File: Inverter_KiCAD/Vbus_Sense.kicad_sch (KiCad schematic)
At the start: 9 parts, among them U12 HCPL-7800A

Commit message: assigments footprints
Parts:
- removed U5: ~, symbol MPRB2415S-6W:MPRB2415S-6W
- C10: footprint (none) -> Capacitor_SMD:CP_Elec_6.3x7.7; MFR (none) -> 865060445005
- C19: footprint (none) -> Capacitor_SMD:CP_Elec_5x5.4; MFR (none) -> 865060442002
- C24, C27, C30: footprint (none) -> Capacitor_SMD:C_0603_1608Metric_Pad1.08x0.95mm_HandSolder
- R13, R16: footprint (none) -> Resistor_SMD:R_0603_1608Metric_Pad0.98x0.95mm_HandSolder
- U12: footprint 300mil_DIP-8_BRA -> HCPL-7800A:HCPL-7800A
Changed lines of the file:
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@@
       (effects (font (size 1.27 1.27)) (justify left))
     )
-    (property "Footprint" "" (at 118.11 73.66 0)
+    (property "Footprint" "Capacitor_SMD:C_0603_1608Metric_Pad1.08x0.95mm_HandSolder" (at 118.11 73.66 0)
       (effects (font (size 1.27 1.27)) hide)
     )
@@
         )
         (path "/5e6c1e3f-0815-454a-8acb-8e3e2d064875/68381f6c-5b48-4aca-8792-bde0d1e54d5e"
-          (reference "C33") (unit 1)
+          (reference "C35") (unit 1)
         )
       )
@@
         )
         (path "/5e6c1e3f-0815-454a-8acb-8e3e2d064875/68381f6c-5b48-4aca-8792-bde0d1e54d5e"
-          (reference "#PWR023") (unit 1)
+          (reference "#PWR036") (unit 1)
         )
       )
@@
       (effects (font (size 1.27 1.27)) (justify left))
     )
-    (property "Footprint" "" (at 47.9552 104.14 0)
+    (property "Footprint" "Capacitor_SMD:CP_Elec_6.3x7.7" (at 47.9552 104.14 0)
       (effects (font (size 1.27 1.27)) hide)
     )
@@
       (effects (font (size 1.27 1.27)) hide)
     )
+    (property "MFR" "865060445005" (at 46.99 100.33 0)
+      (effects (font (size 1.27 1.27)) hide)
+    )
     (pin "1")
     (pin "2")
@@
         )
         (path "/5e6c1e3f-0815-454a-8acb-8e3e2d064875/68381f6c-5b48-4aca-8792-bde0d1e54d5e"
-          (reference "C36") (unit 1)
+          (reference "C33") (unit 1)
         )
       )
@@
         )
         (path "/5e6c1e3f-0815-454a-8acb-8e3e2d064875/68381f6c-5b48-4aca-8792-bde0d1e54d5e"
-          (reference "#PWR045") (unit 1)
+          (reference "#PWR032") (unit 1)
         )
       )
@@
       (effects (font (size 1.524 1.524)))
     )
-    (property "Footprint" "300mil_DIP-8_BRA" (at 146.05 85.09 0)
+    (property "Footprint" "HCPL-7800A:HCPL-7800A" (at 146.05 85.09 0)
       (effects (font (size 1.27 1.27) italic) hide)
     )
@@
         )
         (path "/5e6c1e3f-0815-454a-8acb-8e3e2d064875/68381f6c-5b48-4aca-8792-bde0d1e54d5e"
-          (reference "U15") (unit 1)
+          (reference "U16") (unit 1)
         )
       )
@@
   (symbol (lib_id "power:+5V") (at 82.55 77.47 270) (unit 1)
     (in_bom yes) (on_board yes) (dnp no) (fields_autoplaced)
-    (property "Reference" "#PWR022" (at 78.74 77.47 0)
+    (property "Reference" "#PWR033" (at 78.74 77.47 0)
       (effects (font (size 1.27 1.27)) hide)
     )
@@
       (project "Inverter_KiCAD"
         (path "/5e6c1e3f-0815-454a-8acb-8e3e2d064875/68381f6c-5b48-4aca-8792-bde0d1e54d5e"
-          (reference "#PWR022") (unit 1)
+          (reference "#PWR033") (unit 1)
         )
       )
@@
         )
         (path "/5e6c1e3f-0815-454a-8acb-8e3e2d064875/68381f6c-5b48-4aca-8792-bde0d1e54d5e"
-          (reference "#PWR043") (unit 1)
+          (reference "#PWR038") (unit 1)
         )
       )
@@
       (effects (font (size 1.27 1.27)) (justify left))
     )
-    (property "Footprint" "" (at 105.41 64.77 0)
+    (property "Footprint" "Resistor_SMD:R_0603_1608Metric_Pad0.98x0.95mm_HandSolder" (at 105.41 64.77 0)
       (effects (font (size 1.27 1.27)) hide)
     )
@@
       (effects (font (size 1.27 1.27)) (justify left))
     )
-    (property "Footprint" "" (at 152.4 100.33 0)
+    (property "Footprint" "Capacitor_SMD:C_0603_1608Metric_Pad1.08x0.95mm_HandSolder" (at 152.4 100.33 0)
       (effects (font (size 1.27 1.27)) hide)
     )
@@
         )
         (path "/5e6c1e3f-0815-454a-8acb-8e3e2d064875/68381f6c-5b48-4aca-8792-bde0d1e54d5e"
-          (reference "C34") (unit 1)
+          (reference "C36") (unit 1)
         )
       )
@@
         )
         (path "/5e6c1e3f-0815-454a-8acb-8e3e2d064875/68381f6c-5b48-4aca-8792-bde0d1e54d5e"
-          (reference "#PWR021") (unit 1)
+          (reference "#PWR035") (unit 1)
         )
       )
@@
       (effects (font (size 1.27 1.27)) (justify left))
     )
-    (property "Footprint" "" (at 105.41 72.39 0)
+    (property "Footprint" "Resistor_SMD:R_0603_1608Metric_Pad0.98x0.95mm_HandSolder" (at 105.41 72.39 0)
       (effects (font (size 1.27 1.27)) hide)
     )
@@
         )
         (path "/5e6c1e3f-0815-454a-8acb-8e3e2d064875/68381f6c-5b48-4aca-8792-bde0d1e54d5e"
-          (reference "#PWR042") (unit 1)
+          (reference "#PWR037") (unit 1)
         )
       )
@@
         )
         (path "/5e6c1e3f-0815-454a-8acb-8e3e2d064875/68381f6c-5b48-4aca-8792-bde0d1e54d5e"
-          (reference "#PWR044") (unit 1)
+          (reference "#PWR034") (unit 1)
         )
       )
@@
       (effects (font (size 1.27 1.27)) (justify left))
     )
-    (property "Footprint" "" (at 67.0052 85.09 0)
+    (property "Footprint" "Capacitor_SMD:CP_Elec_5x5.4" (at 67.0052 85.09 0)
       (effects (font (size 1.27 1.27)) hide)
     )
@@
       (effects (font (size 1.27 1.27)) hide)
     )
+    (property "MFR" "865060442002" (at 66.04 81.28 0)
+      (effects (font (size 1.27 1.27)) hide)
+    )
     (pin "1")
     (pin "2")
@@
         )
         (path "/5e6c1e3f-0815-454a-8acb-8e3e2d064875/68381f6c-5b48-4aca-8792-bde0d1e54d5e"
-          (reference "C38") (unit 1)
+          (reference "C34") (unit 1)
         )
       )
@@
       (effects (font (size 1.27 1.27)) (justify left))
     )
-    (property "Footprint" "" (at 162.56 100.33 0)
+    (property "Footprint" "Capacitor_SMD:C_0603_1608Metric_Pad1.08x0.95mm_HandSolder" (at 162.56 100.33 0)
       (effects (font (size 1.27 1.27)) hide)
     )
@@
         )
         (path "/5e6c1e3f-0815-454a-8acb-8e3e2d064875/68381f6c-5b48-4aca-8792-bde0d1e54d5e"
-          (reference "C35") (unit 1)
-        )
-      )
-    )
-  )
-  (symbol (lib_id "MPRB2415S-6W:MPRB2415S-6W") (at 48.26 80.01 0) (unit 1)
-    (in_bom yes) (on_board yes) (dnp no) (fields_autoplaced)
-    (property "Reference" "U5" (at 48.26 69.85 0)
-      (effects (font (size 1.27 1.27)))
-    )
-    (property "Value" "~" (at 48.26 80.01 0)
-      (effects (font (size 1.27 1.27)))
-    )
-    (property "Footprint" "" (at 48.26 80.01 0)
-      (effects (font (size 1.27 1.27)) hide)
-    )
-    (property "Datasheet" "" (at 48.26 80.01 0)
-      (effects (font (size 1.27 1.27)) hide)
-    )
-    (pin "1")
-    (pin "2")
-    (pin "3")
-    (pin "5")
-    (pin "6")
-    (pin "7")
-    (pin "8")
-    (instances
-      (project "Inverter_KiCAD"
-        (path "/5e6c1e3f-0815-454a-8acb-8e3e2d064875/0406dcca-4785-4175-98fc-8c562936c28c"
-          (reference "U5") (unit 1)
-        )
-        (path "/5e6c1e3f-0815-454a-8acb-8e3e2d064875/9da1d24f-0210-4c44-b691-d03fb3165448"
-          (reference "U8") (unit 1)
-        )
-        (path "/5e6c1e3f-0815-454a-8acb-8e3e2d064875/ec1e87e4-c1ff-4173-919d-40f0bb72aaf8"
-          (reference "U3") (unit 1)
-        )
-        (path "/5e6c1e3f-0815-454a-8acb-8e3e2d064875/0e650ff7-9828-4cb9-954d-863730025975"
-          (reference "U9") (unit 1)
-        )
-        (path "/5e6c1e3f-0815-454a-8acb-8e3e2d064875/68381f6c-5b48-4aca-8792-bde0d1e54d5e"
-          (reference "U16") (unit 1)
-        )
-      )
+          (reference "C37") (unit 1)
+        )
+      )

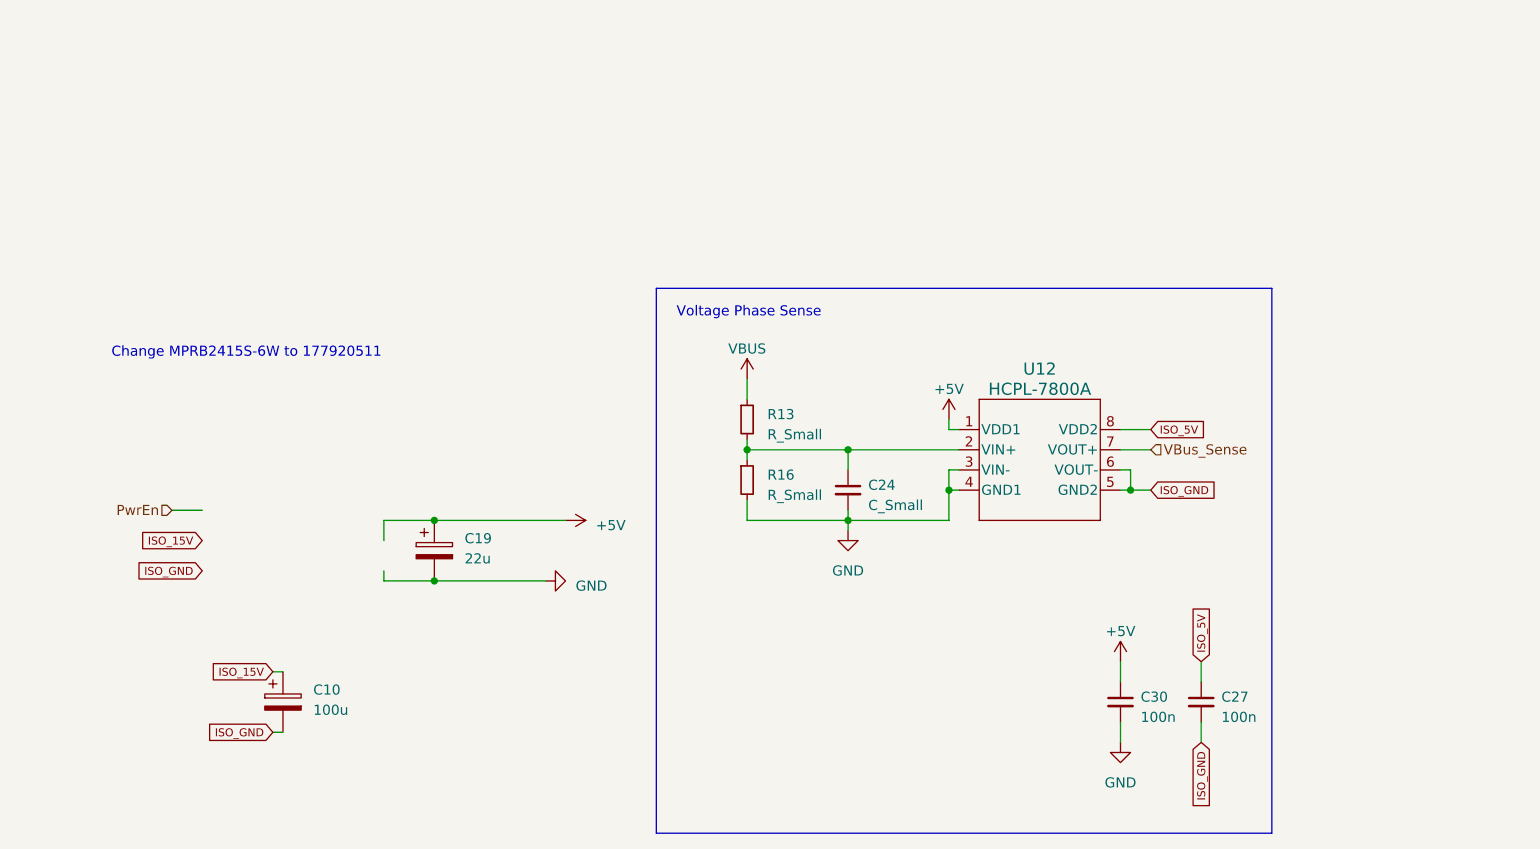
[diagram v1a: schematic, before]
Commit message: update schematic
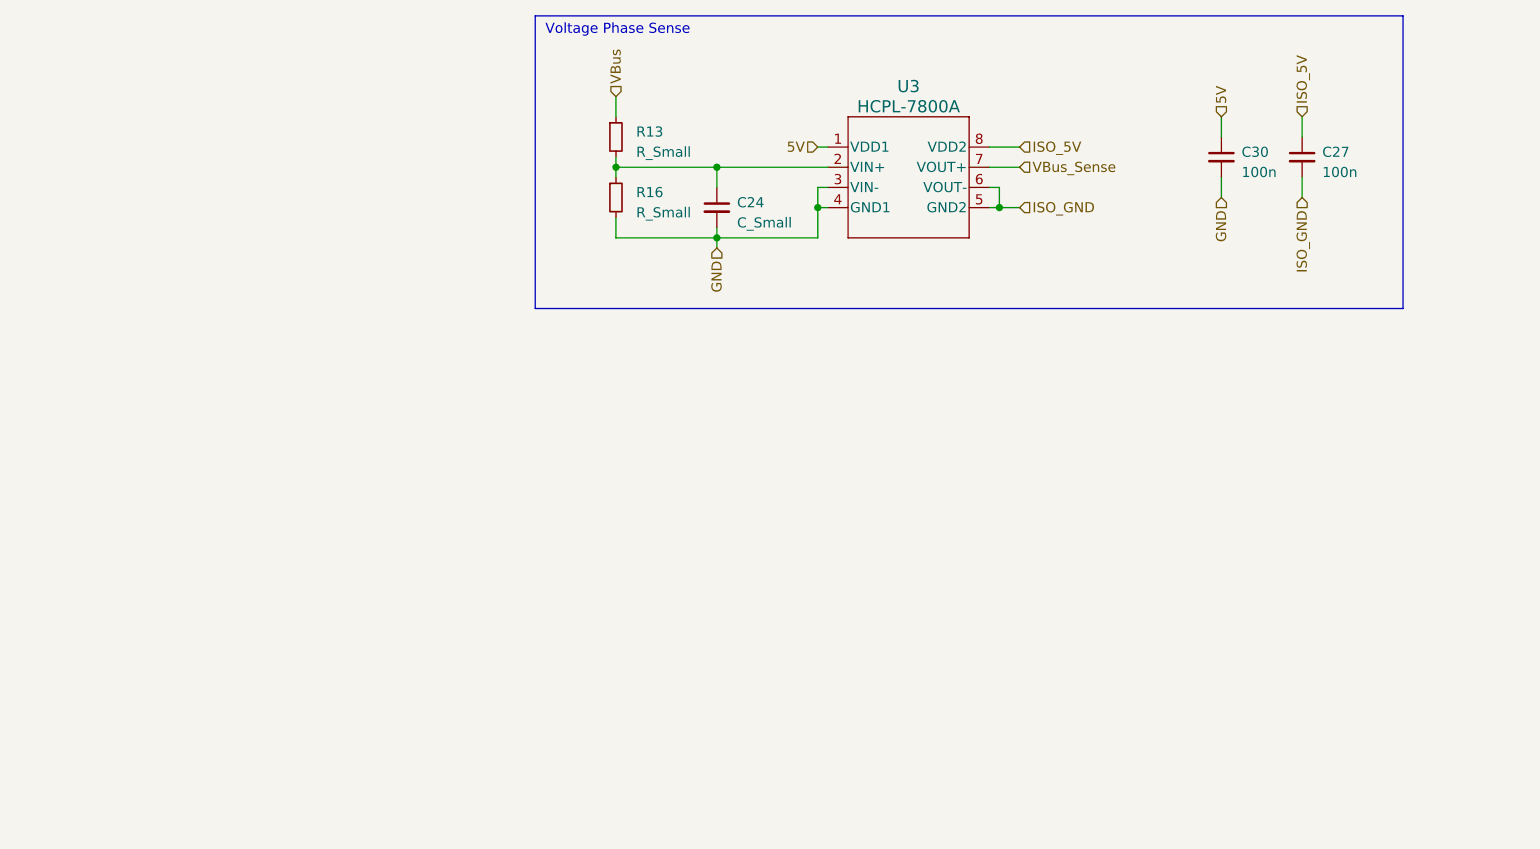
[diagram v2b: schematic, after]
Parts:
- removed C10: 100u, Capacitor_SMD:CP_Elec_6.3x7.7, symbol Device:C_Polarized
- removed C19: 22u, Capacitor_SMD:CP_Elec_5x5.4, symbol Device:C_Polarized
- removed U12: HCPL-7800A, HCPL-7800A:HCPL-7800A, symbol HCPL-7800A:HCPL-7800A
- added U3: HCPL-7800A, Custom:HCPL-7800A, symbol Custom:HCPL-7800A
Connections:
- net GND: now also U3.3 (VIN-), U3.4 (GND1)
- net ISO_5V: now also U3.8 (VDD2)
- net ISO_GND: now also U3.5 (GND2), U3.6 (VOUT-)
- net VBus_Sense: now also U3.7 (VOUT+)
- net at C24.1, R13.2, R16.1: now also U3.2 (VIN+)
- net +5V renamed 5V
- net 5V: now also U3.1 (VDD1)
- net VBUS renamed VBus
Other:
- note removed: "Change MPRB2415S-6W to 177920511"
- moved on the sheet: C24, C27, C30, R13, R16

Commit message: add break
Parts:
- added C10, C8, C9: 4.7n, Capacitor_SMD:C_0402_1005Metric_Pad0.74x0.62mm_HandSolder, symbol Device:C_Small
- added U6: GO 10-SME/SP3, Custom:SOIC8-GO-SME&slash_SP3_LEM, symbol Custom:GO_10-SME
- C27, C30: footprint Capacitor_SMD:C_0603_1608Metric_Pad1.08x0.95mm_HandSolder -> Capacitor_SMD:C_0402_1005Metric_Pad0.74x0.62mm_HandSolder
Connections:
- net ISO_GND: now also C10.2, C8.2, C9.2, U6.5 (GND)
- net VBus renamed V_Bus_Out
- net V_Bus_Out: now also U6.3 (IP-), U6.4 (IP-)
- new net ISO_3.3V: C8.1, U6.8 (UC)
- new net Imes: C9.1, U6.7 (UOUT)
- new net Uref: C10.1, U6.6 (UREF)
- new net V_Bus_In: U6.1 (IP+), U6.2 (IP+)
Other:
- note added: "Hall current"
- moved on the sheet: C24, C27, C30, R13, R16, U3

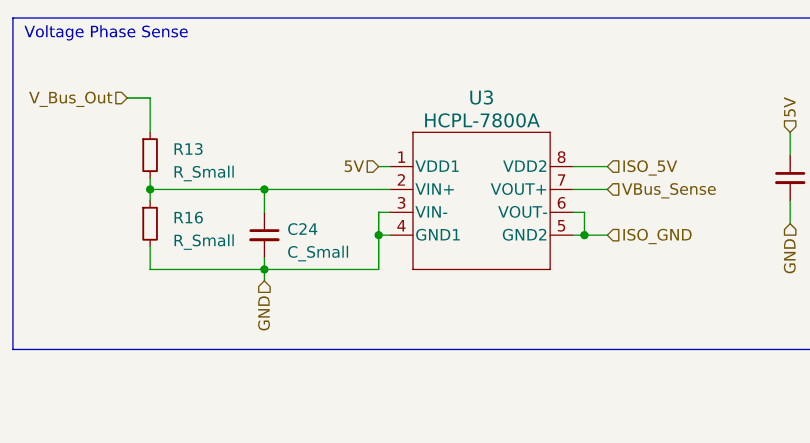
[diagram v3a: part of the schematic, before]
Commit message: start schematic Nucleo board
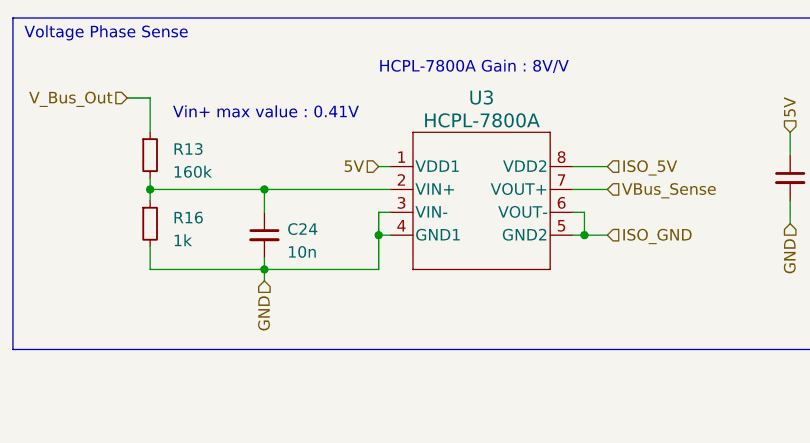
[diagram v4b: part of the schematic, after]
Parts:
- C24: value C_Small -> 10n
- R13: value R_Small -> 160k
- R16: value R_Small -> 1k
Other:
- note added: "HCPL-7800A Gain : 8V/V"
- note added: "Vin+ max value : 0.41V"
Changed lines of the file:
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@@
+    (effects (font (size 1.27 1.27)) (justify left bottom))
+  )
+  (text "Vin+ max value : 0.41V" (at 111.76 25.4 0)
+    (effects (font (size 1.27 1.27)) (justify left bottom))
+  )
+  (text "HCPL-7800A Gain : 8V/V" (at 134.62 20.32 0)
     (effects (font (size 1.27 1.27)) (justify left bottom))
   )
@@
       (effects (font (size 1.27 1.27)) (justify left))
     )
-    (property "Value" "C_Small" (at 124.46 40.0113 0)
+    (property "Value" "10n" (at 124.46 40.0113 0)
       (effects (font (size 1.27 1.27)) (justify left))
     )
@@
       (effects (font (size 1.27 1.27)) (justify left))
     )
-    (property "Value" "R_Small" (at 111.76 31.115 0)
+    (property "Value" "160k" (at 111.76 31.115 0)
       (effects (font (size 1.27 1.27)) (justify left))
     )
@@
       (effects (font (size 1.27 1.27)) (justify left))
     )
-    (property "Value" "R_Small" (at 111.76 38.735 0)
+    (property "Value" "1k" (at 111.76 38.735 0)
       (effects (font (size 1.27 1.27)) (justify left))
     )
